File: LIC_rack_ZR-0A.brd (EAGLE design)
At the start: 110 x 90.8 mm, 57 parts, among them IC1 ATMEGA644A, IC2 MAX481CSA, IC3 FT232RL, J1 J_1206, J2 J_1206, J3 J_1206, J4 J_1206, P1 PT6VK010, Q1 14.7456MHz, X1 MINI-USB-SCHIELD-32005-201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

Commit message: Uprava desek
Uprava desek a pouziti autorouteru pro verzi 01
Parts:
- moved R6 144.9 mm to (50.1, 32.7), turned to 180 degrees
- moved R8 137.8 mm to (46.1, 48.1), turned to 180 degrees
- moved R5 135.8 mm to (43.2, 32.7), turned to 180 degrees
- moved R9 130.5 mm to (39.4, 48.0), turned to 180 degrees
- moved R4 128.8 mm to (30.3, 30.2), turned to 90 degrees
- moved R7 120.5 mm to (29.1, 48.0)
- moved R14 118.4 mm to (19.1, 41.2), turned to 90 degrees
- moved C13 116.4 mm to (23.3, 30.2), flipped to the bottom, turned to 270 degrees
- moved C12 96.4 mm to (47.9, 21.3), flipped to the bottom
- moved C11 93.7 mm to (56.9, 13.2), flipped to the bottom, turned to 270 degrees
- moved C14 85.1 mm to (60.1, 13.2), flipped to the bottom, turned to 270 degrees
- moved D2 42.3 mm to (19.6, 6.50), turned to 90 degrees
- moved R13 40.1 mm to (19.6, 12.0), turned to 270 degrees
- moved D1 34.8 mm to (22.4, 6.50), turned to 90 degrees
- moved R12 31.5 mm to (22.4, 12.0), turned to 270 degrees
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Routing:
- net EXT_RS485-: track 0.00 -> 1447.1 mm
- net MODUL_RST: track 0.00 -> 1312.2 mm
- net SYNC16: track 0.00 -> 1177.1 mm
- net SYNC15: track 0.00 -> 1055.1 mm
- net SYNC14: track 0.00 -> 974.5 mm
- net SYNC13: track 0.00 -> 888.9 mm
- net SYNC12: track 0.00 -> 824.7 mm
- net SYNC11: track 0.00 -> 766.3 mm
- net SYNC10: track 0.00 -> 696.0 mm
- net SYNC09: track 0.00 -> 637.7 mm
- net SYNC08: track 0.00 -> 599.5 mm
- net SYNC07: track 0.00 -> 557.8 mm
- net SYNC06: track 0.00 -> 522.8 mm
- net +5V: track 9.70 -> 517.2 mm, vias 3 -> 9
- net SYNC05: track 0.00 -> 477.0 mm
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- added copper zone on layer 1, net GNDINT
- added copper zone on layer 16, net GNDINT

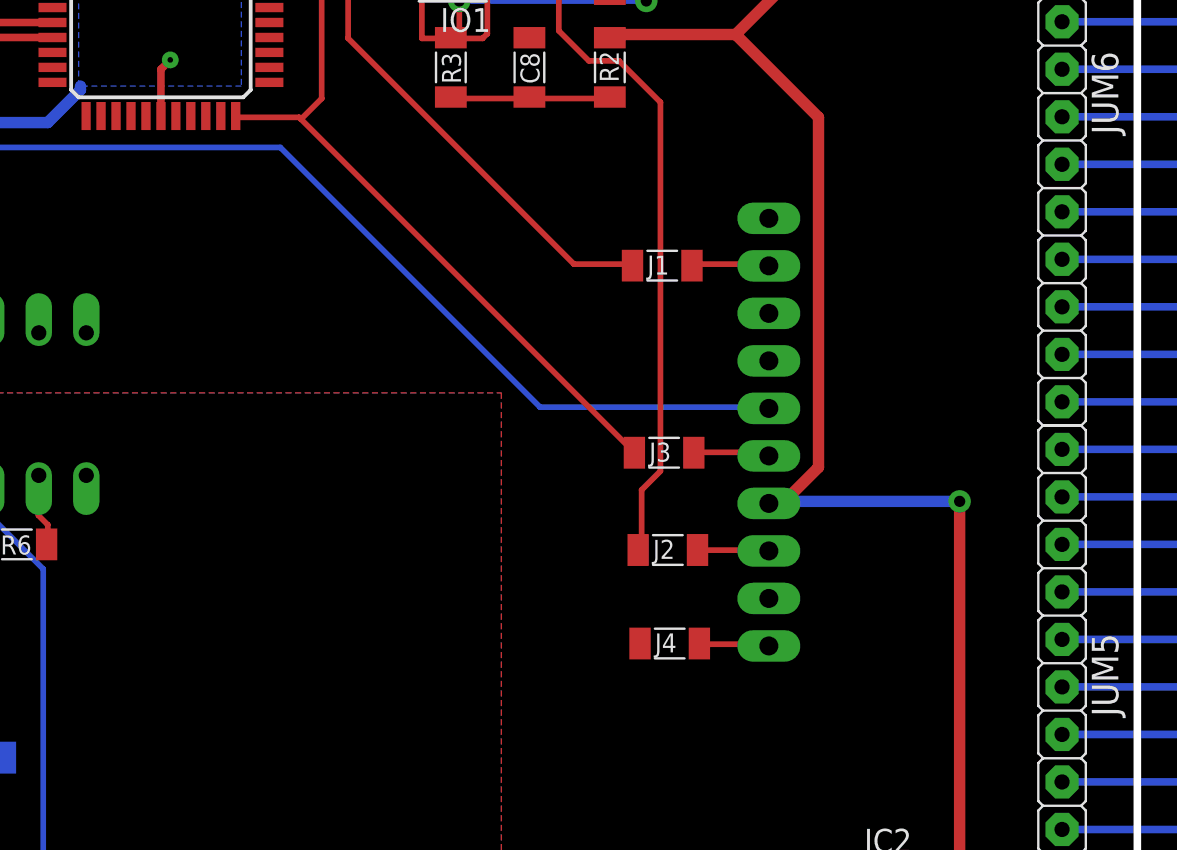
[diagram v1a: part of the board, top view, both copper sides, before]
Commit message: Uprava desky
Pridán signál pro resetování modulů....
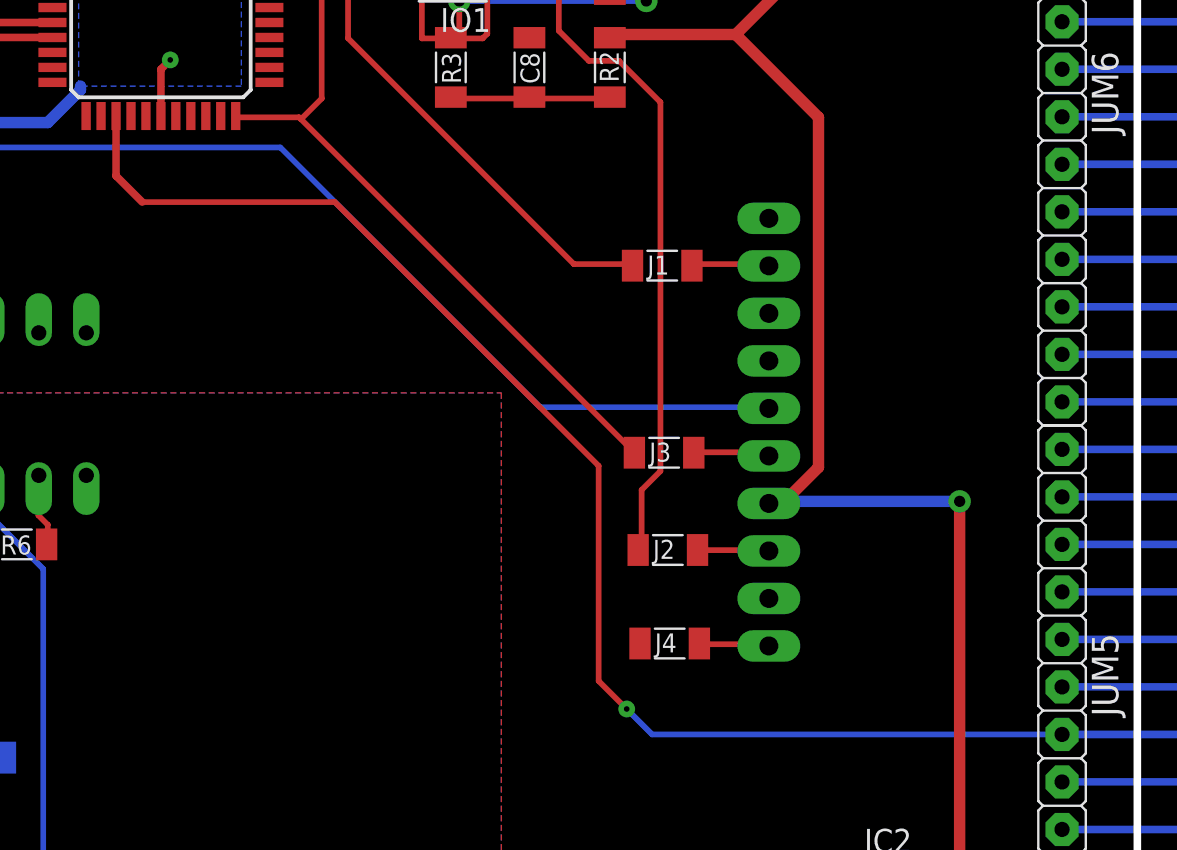
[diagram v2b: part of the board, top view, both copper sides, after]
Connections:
- net MODUL_RST: now also IC1.14
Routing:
- net MODUL_RST: track 1312.2 -> 1385.1 mm, vias 0 -> 1
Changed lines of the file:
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@@
 <wire x1="367.8" y1="283.7" x2="367.8" y2="233.8" width="0.4064" layer="16"/>
 <wire x1="367.8" y1="233.8" x2="156.54" y2="22.54" width="0.4064" layer="16"/>
+<contactref element="IC1" pad="14"/>
+<wire x1="55.4" y1="55.6" x2="55.4" y2="52.4" width="0.4064" layer="1"/>
+<wire x1="55.4" y1="52.4" x2="56.8" y2="51" width="0.4064" layer="1"/>
+<wire x1="56.8" y1="51" x2="67.1" y2="51" width="0.3048" layer="1"/>
+<wire x1="67.1" y1="51" x2="81.2" y2="36.9" width="0.3048" layer="1"/>
+<wire x1="81.2" y1="36.9" x2="81.2" y2="25.4" width="0.3048" layer="1"/>
+<wire x1="81.2" y1="25.4" x2="82.7" y2="23.9" width="0.3048" layer="1"/>
+<wire x1="105.975" y1="22.54" x2="84.06" y2="22.54" width="0.3048" layer="16"/>
+<wire x1="84.06" y1="22.54" x2="82.7" y2="23.9" width="0.3048" layer="16"/>
+<via x="82.7" y="23.9" extent="1-16" drill="0.3"/>
 </signal>
 <signal name="EXT_RS485+">
